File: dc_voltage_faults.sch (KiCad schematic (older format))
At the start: 4 parts

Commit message: Adds todos.
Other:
- note added: "TODO(willjschmitt): Set VDC_OV_REF and VDC_UV_REF."
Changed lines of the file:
@@
 	2900 2200 2900 1200
 Connection ~ 2900 1200
+Text Notes 2800 750  0    60   ~ 0
+TODO(willjschmitt): Set VDC_OV_REF and VDC_UV_REF.
 $EndSCHEMATC

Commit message: Annotate and add negative IOC faults.
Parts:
- gave numbers to parts that had none: 2
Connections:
- net DC_UV_FAULT: now also U11.7; no longer U11.1
- net VDC_UV_REF: now also U11.6 (_); no longer U11.2 (_)
- net V_DC: now also U11.5 (+); no longer U11.3 (+)
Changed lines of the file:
@@
 DC_UV_FAULT
 $Comp
-L LMV393 U?
+L LMV393 U11
 U 1 1 5AFAD9C3
 P 4150 1300
-F 0 "U?" H 4300 1450 50  0000 C CNN
+F 0 "U11" H 4300 1450 50  0000 C CNN
 F 1 "LMV393" H 4400 1150 50  0000 C CNN
 F 2 "" H 4150 1300 50  0001 C CNN
@@
 $EndComp
 $Comp
-L LMV393 U?
-U 1 1 5AFAD9CA
+L LMV393 U11
+U 2 1 5AFAD9CA
 P 4150 2300
-F 0 "U?" H 4300 2450 50  0000 C CNN
+F 0 "U11" H 4300 2450 50  0000 C CNN
 F 1 "LMV393" H 4400 2150 50  0000 C CNN
 F 2 "" H 4150 2300 50  0001 C CNN
 F 3 "" H 4150 2300 50  0001 C CNN
-	1    4150 2300
+	2    4150 2300
 	1    0    0    -1
 $EndComp
 $Comp
-L LMV393 U?
+L LMV393 U12
 U 1 1 5AFAD9D1
 P 4150 3300
-F 0 "U?" H 4300 3450 50  0000 C CNN
+F 0 "U12" H 4300 3450 50  0000 C CNN
 F 1 "LMV393" H 4400 3150 50  0000 C CNN
 F 2 "" H 4150 3300 50  0001 C CNN
@@
 $EndComp
 $Comp
-L LMV393 U?
-U 1 1 5AFAD9D8
+L LMV393 U12
+U 2 1 5AFAD9D8
 P 4150 4300
-F 0 "U?" H 4300 4450 50  0000 C CNN
+F 0 "U12" H 4300 4450 50  0000 C CNN
 F 1 "LMV393" H 4400 4150 50  0000 C CNN
 F 2 "" H 4150 4300 50  0001 C CNN
 F 3 "" H 4150 4300 50  0001 C CNN
-	1    4150 4300
+	2    4150 4300
 	1    0    0    -1
 $EndComp
 $Comp
-L GND #PWR?
+L GND #PWR76
 U 1 1 5AFAD9DF
 P 4050 2600
-F 0 "#PWR?" H 4050 2350 50  0001 C CNN
+F 0 "#PWR76" H 4050 2350 50  0001 C CNN
 F 1 "GND" H 4050 2450 50  0000 C CNN
 F 2 "" H 4050 2600 50  0001 C CNN
@@
 $EndComp
 $Comp
-L GND #PWR?
+L GND #PWR74
 U 1 1 5AFAD9E5
 P 4050 1600
-F 0 "#PWR?" H 4050 1350 50  0001 C CNN
+F 0 "#PWR74" H 4050 1350 50  0001 C CNN
 F 1 "GND" H 4050 1450 50  0000 C CNN
 F 2 "" H 4050 1600 50  0001 C CNN
@@
 $EndComp
 $Comp
-L GND #PWR?
+L GND #PWR78
 U 1 1 5AFAD9EB
 P 4050 3600
-F 0 "#PWR?" H 4050 3350 50  0001 C CNN
+F 0 "#PWR78" H 4050 3350 50  0001 C CNN
 F 1 "GND" H 4050 3450 50  0000 C CNN
 F 2 "" H 4050 3600 50  0001 C CNN
@@
 $EndComp
 $Comp
-L GND #PWR?
+L GND #PWR80
 U 1 1 5AFAD9F1
 P 4050 4600
-F 0 "#PWR?" H 4050 4350 50  0001 C CNN
+F 0 "#PWR80" H 4050 4350 50  0001 C CNN
 F 1 "GND" H 4050 4450 50  0000 C CNN
 F 2 "" H 4050 4600 50  0001 C CNN
@@
 	3650 2400 3850 2400
 $Comp
-L +5V #PWR?
+L +5V #PWR73
 U 1 1 5AFADA00
 P 4050 1000
-F 0 "#PWR?" H 4050 850 50  0001 C CNN
+F 0 "#PWR73" H 4050 850 50  0001 C CNN
 F 1 "+5V" H 4050 1140 50  0000 C CNN
 F 2 "" H 4050 1000 50  0001 C CNN
@@
 $EndComp
 $Comp
-L +5V #PWR?
+L +5V #PWR75
 U 1 1 5AFADA06
 P 4050 2000
-F 0 "#PWR?" H 4050 1850 50  0001 C CNN
+F 0 "#PWR75" H 4050 1850 50  0001 C CNN
 F 1 "+5V" H 4050 2140 50  0000 C CNN
 F 2 "" H 4050 2000 50  0001 C CNN
@@
 $EndComp
 $Comp
-L +5V #PWR?
+L +5V #PWR77
 U 1 1 5AFADA0C
 P 4050 3000
-F 0 "#PWR?" H 4050 2850 50  0001 C CNN
+F 0 "#PWR77" H 4050 2850 50  0001 C CNN
 F 1 "+5V" H 4050 3140 50  0000 C CNN
 F 2 "" H 4050 3000 50  0001 C CNN
@@
 $EndComp
 $Comp
-L +5V #PWR?
+L +5V #PWR79
 U 1 1 5AFADA12
 P 4050 4000
-F 0 "#PWR?" H 4050 3850 50  0001 C CNN
+F 0 "#PWR79" H 4050 3850 50  0001 C CNN
 F 1 "+5V" H 4050 4140 50  0000 C CNN
 F 2 "" H 4050 4000 50  0001 C CNN

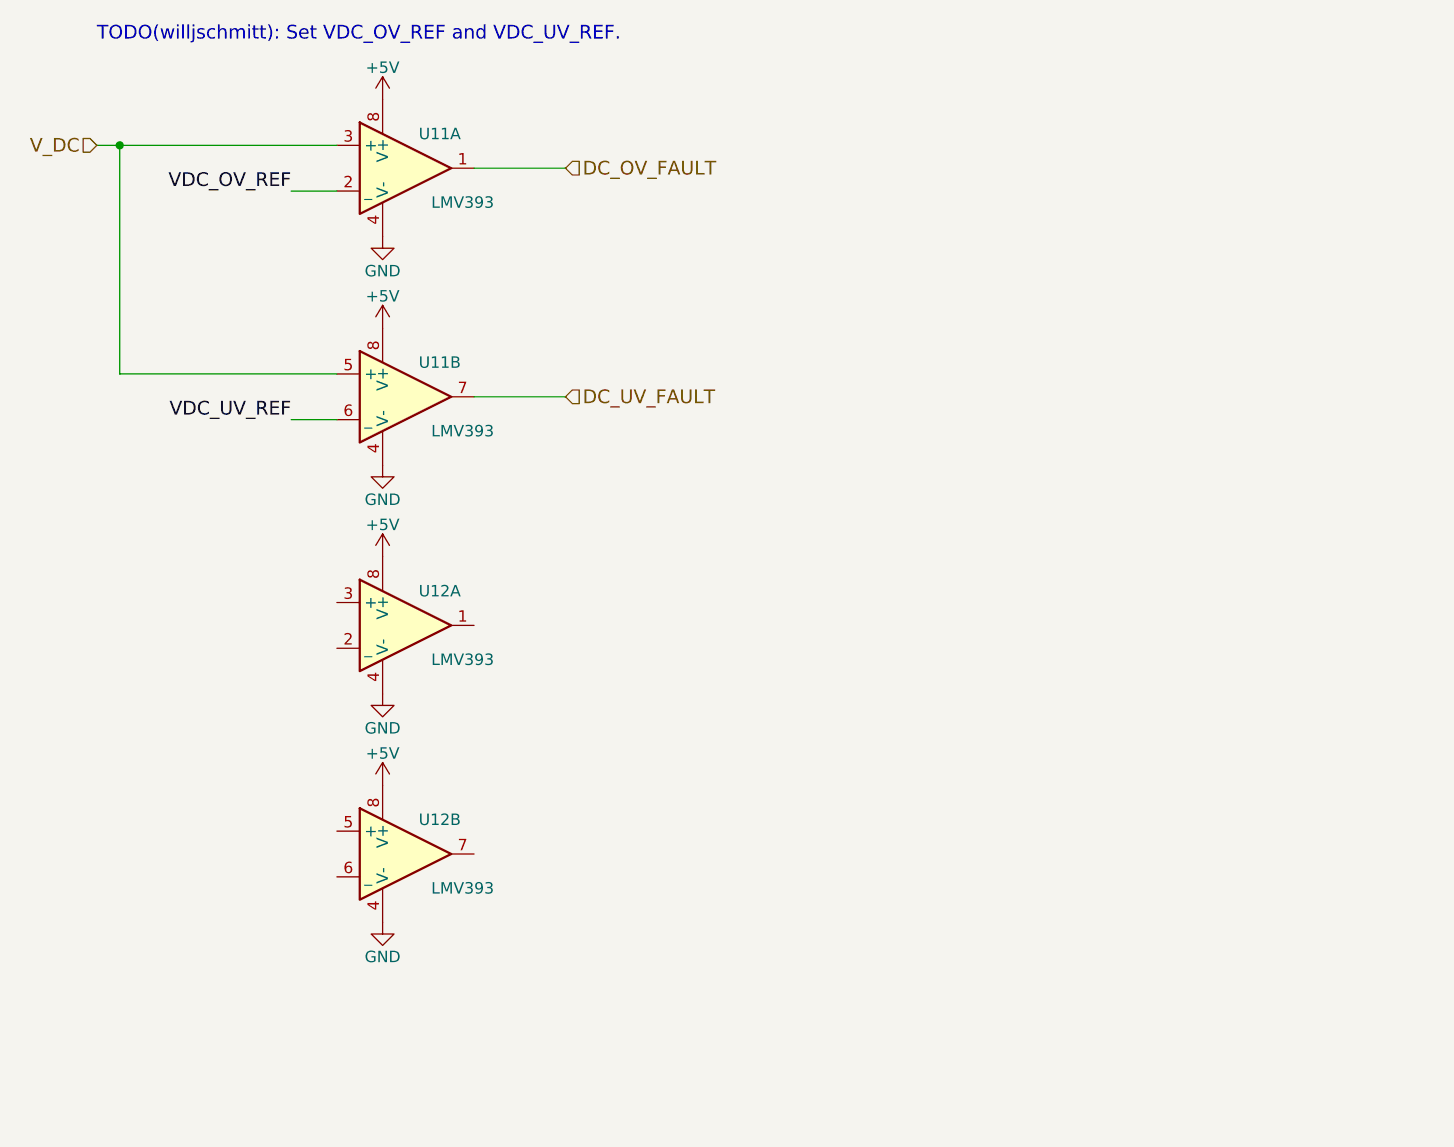
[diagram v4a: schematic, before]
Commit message: Adding DC ov/uv set points
Also corrected DC UV comparator.
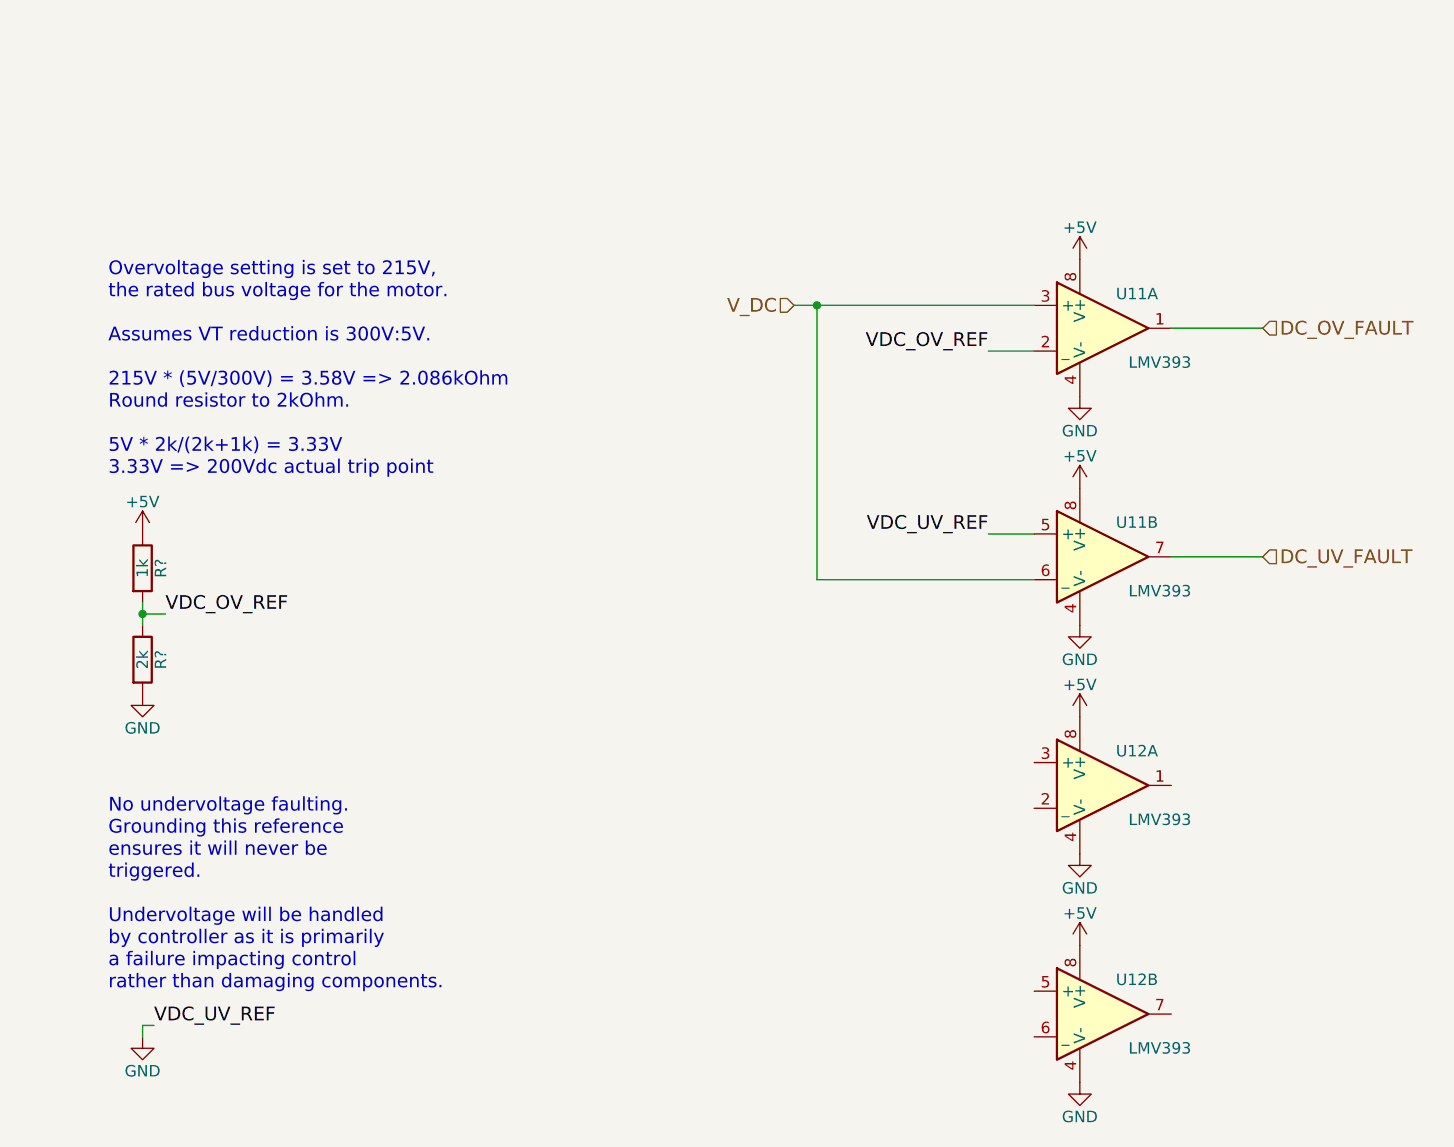
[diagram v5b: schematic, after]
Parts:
- added R?: 1k, symbol R
- added R?: 2k, symbol R
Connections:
- net VDC_UV_REF is gone; now on net V_DC: U11.6 (_)
- net +5V: now also R?.1
- net GND: now also U11.5 (+), R?.2
- net VDC_OV_REF: now also R?.1, R?.2
- net V_DC: no longer U11.5 (+)
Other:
- note added: "No undervoltage faulting.\nGrounding this reference\nensures it will never be\ntriggered.\n\nUndervoltage will be handled\nby controller as it is primarily\na failure impacting control\nrather than damaging components."
- note added: "Overvoltage setting is set to 215V,\nthe rated bus voltage for the motor.\n\nAssumes VT reduction is 300V:5V.\n\n215V * (5V/300V) = 3.58V => 2.086kOhm\nRound resistor to 2kOhm.\n\n5V * 2k/(2k+1k) = 3.33V\n3.33V => 200Vdc actual trip point"
- note removed: "TODO(willjschmitt): Set VDC_OV_REF and VDC_UV_REF."
- moved on the sheet: U11A, U11B, U12A, U12B

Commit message: Deduping kty_84 sheet names.
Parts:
- gave numbers to parts that had none: 2
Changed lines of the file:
@@
 $EndComp
 $Comp
-L GND #PWR76
+L GND #PWR077
 U 1 1 5AFAD9DF
 P 7100 3300
-F 0 "#PWR76" H 7100 3050 50  0001 C CNN
+F 0 "#PWR077" H 7100 3050 50  0001 C CNN
 F 1 "GND" H 7100 3150 50  0000 C CNN
 F 2 "" H 7100 3300 50  0001 C CNN
@@
 $EndComp
 $Comp
-L GND #PWR74
+L GND #PWR078
 U 1 1 5AFAD9E5
 P 7100 2300
-F 0 "#PWR74" H 7100 2050 50  0001 C CNN
+F 0 "#PWR078" H 7100 2050 50  0001 C CNN
 F 1 "GND" H 7100 2150 50  0000 C CNN
 F 2 "" H 7100 2300 50  0001 C CNN
@@
 $EndComp
 $Comp
-L GND #PWR78
+L GND #PWR079
 U 1 1 5AFAD9EB
 P 7100 4300
-F 0 "#PWR78" H 7100 4050 50  0001 C CNN
+F 0 "#PWR079" H 7100 4050 50  0001 C CNN
 F 1 "GND" H 7100 4150 50  0000 C CNN
 F 2 "" H 7100 4300 50  0001 C CNN
@@
 $EndComp
 $Comp
-L GND #PWR80
+L GND #PWR080
 U 1 1 5AFAD9F1
 P 7100 5300
-F 0 "#PWR80" H 7100 5050 50  0001 C CNN
+F 0 "#PWR080" H 7100 5050 50  0001 C CNN
 F 1 "GND" H 7100 5150 50  0000 C CNN
 F 2 "" H 7100 5300 50  0001 C CNN
@@
 VDC_UV_REF
 $Comp
-L +5V #PWR73
+L +5V #PWR081
 U 1 1 5AFADA00
 P 7100 1700
-F 0 "#PWR73" H 7100 1550 50  0001 C CNN
+F 0 "#PWR081" H 7100 1550 50  0001 C CNN
 F 1 "+5V" H 7100 1840 50  0000 C CNN
 F 2 "" H 7100 1700 50  0001 C CNN
@@
 $EndComp
 $Comp
-L +5V #PWR75
+L +5V #PWR082
 U 1 1 5AFADA06
 P 7100 2700
-F 0 "#PWR75" H 7100 2550 50  0001 C CNN
+F 0 "#PWR082" H 7100 2550 50  0001 C CNN
 F 1 "+5V" H 7100 2840 50  0000 C CNN
 F 2 "" H 7100 2700 50  0001 C CNN
@@
 $EndComp
 $Comp
-L +5V #PWR77
+L +5V #PWR083
 U 1 1 5AFADA0C
 P 7100 3700
-F 0 "#PWR77" H 7100 3550 50  0001 C CNN
+F 0 "#PWR083" H 7100 3550 50  0001 C CNN
 F 1 "+5V" H 7100 3840 50  0000 C CNN
 F 2 "" H 7100 3700 50  0001 C CNN
@@
 $EndComp
 $Comp
-L +5V #PWR79
+L +5V #PWR084
 U 1 1 5AFADA12
 P 7100 4700
-F 0 "#PWR79" H 7100 4550 50  0001 C CNN
+F 0 "#PWR084" H 7100 4550 50  0001 C CNN
 F 1 "+5V" H 7100 4840 50  0000 C CNN
 F 2 "" H 7100 4700 50  0001 C CNN
@@
 Connection ~ 5950 1900
 $Comp
-L GND #PWR?
+L GND #PWR085
 U 1 1 5AF048F7
 P 3000 5100
-F 0 "#PWR?" H 3000 4850 50  0001 C CNN
+F 0 "#PWR085" H 3000 4850 50  0001 C CNN
 F 1 "GND" H 3000 4950 50  0000 C CNN
 F 2 "" H 3000 5100 50  0001 C CNN
@@
 $EndComp
 $Comp
-L +5V #PWR?
+L +5V #PWR086
 U 1 1 5AF04913
 P 3000 2900
-F 0 "#PWR?" H 3000 2750 50  0001 C CNN
+F 0 "#PWR086" H 3000 2750 50  0001 C CNN
 F 1 "+5V" H 3000 3040 50  0000 C CNN
 F 2 "" H 3000 2900 50  0001 C CNN
@@
 VDC_UV_REF
 $Comp
-L GND #PWR?
+L GND #PWR087
 U 1 1 5AF04957
 P 3000 3600
-F 0 "#PWR?" H 3000 3350 50  0001 C CNN
+F 0 "#PWR087" H 3000 3350 50  0001 C CNN
 F 1 "GND" H 3000 3450 50  0000 C CNN
 F 2 "" H 3000 3600 50  0001 C CNN
@@
 $EndComp
 $Comp
-L R R?
+L R R23
 U 1 1 5AF0496C
 P 3000 3050
-F 0 "R?" V 3080 3050 50  0000 C CNN
+F 0 "R23" V 3080 3050 50  0000 C CNN
 F 1 "1k" V 3000 3050 50  0000 C CNN
 F 2 "" V 2930 3050 50  0001 C CNN
@@
 $EndComp
 $Comp
-L R R?
+L R R24
 U 1 1 5AF049B3
 P 3000 3450
-F 0 "R?" V 3080 3450 50  0000 C CNN
+F 0 "R24" V 3080 3450 50  0000 C CNN
 F 1 "2k" V 3000 3450 50  0000 C CNN
 F 2 "" V 2930 3450 50  0001 C CNN
